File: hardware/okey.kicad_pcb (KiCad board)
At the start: 2 copper layers, 263.4 x 349.9 mm, 158 parts, among them IC1 4094N, IC2 4094N, P1 ROW_JMP, P10 CONN_02X06, P11 CONN_02X06, P12 CONN_02X06, P13 CONN_02X06, P14 CONN_02X06, P15 CONN_02X06, P16 CONN_02X08, P17 CONN_01X01, P18 CONN_02X08, P19 CONN_01X01, P2 CONN_02X13, P20 CONN_01X01, P21 CONN_01X01, P22 CONN_02X08, P23 CONN_02X08, P24 CONN_02X06, P25 CONN_02X06, P26 CONN_02X06, P27 CONN_02X06, P28 CONN_02X06, P29 CONN_02X06, P3 CONN_02X03, P30 CONN_02X08, P31 CONN_02X03, P32 CONN_02X03, P33 CONN_02X06, P34 CONN_02X06, P35 CONN_02X06, P36 CONN_02X06, P37 CONN_02X06, P38 CONN_02X06, P39 CONN_01X01, P4 CONN_02X08, P40 CONN_02X03, P41 CONN_02X06, P42 CONN_02X06, P43 CONN_02X06, P44 CONN_02X06, P45 CONN_02X06, P46 CONN_02X06, P47 CONN_01X01, P48 CONN_02X03, P5 CONN_02X03, P6 CONN_02X10, P7 CONN_02X03, P8 CONN_01X01, P9 CONN_02X08, Q1 Q_NPN_BCE, Q2 Q_NPN_BCE, Q3 Q_NPN_BCE, SW1 MX_D, SW10 MX_D, SW11 MX_D, SW12 MX_D, SW13 MX_D, SW14 MX_D, SW15 MX_D, SW16 MX_D, SW17 MX_D, SW18 MX_D, SW19 SW_PUSH, SW2 MX_D, SW20 SW_PUSH, SW21 SW_PUSH, SW22 SW_PUSH, SW23 SW_PUSH, SW24 SW_PUSH, SW25 SW_PUSH, SW26 SW_PUSH, SW27 SW_PUSH, SW28 SW_PUSH, SW29 SW_PUSH, SW3 MX_D, SW30 SW_PUSH, SW31 SW_PUSH, SW32 SW_PUSH, SW33 SW_PUSH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

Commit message: squash! ... hardware: rework SPI board as SMD board with smaller dimensions ...
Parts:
- added J1: RJ45, Connect:RJ45_8, F.Cu at (63.5, 15.2)
- added J2: RJ45, Connect:RJ45_8, F.Cu at (80.0, 15.2)
- D1, D2, D3, D4, D5, D6, D7, D8: footprint Discret:CP6 -> Discret:D3
- D10, D11, D12, D13, D14, D15, D16, D17, D18, D19, D20, D21, D22, D23, D24, D9: footprint Discret:R4 -> Discret:D4
- moved C1 30.5 mm to (62.9, 62.9)
- moved PNL_ID1 22.2 mm to (106.7, 48.3), turned to 90 degrees
- moved P48 19.4 mm to (109.2, 26.7), turned to 90 degrees
- moved C3 18.1 mm to (50.2, 64.8)
- moved C6 18.1 mm to (77.5, 62.2)
- moved C7 18.1 mm to (77.5, 62.2)
- moved D8 16.6 mm to (124.5, 39.4), turned to 270 degrees
- moved MUX_COL1 14.6 mm to (99.7, 41.3)
- moved P3 14.0 mm to (55.9, 36.8)
- moved U1 14.0 mm to (64.1, 41.3)
- moved P5 14.0 mm to (69.8, 36.8)
- moved C2 13.9 mm to (102.9, 25.4), turned to 270 degrees
- moved D7 13.1 mm to (121.9, 39.4), turned to 270 degrees
- moved P4 10.2 mm to (106.7, 33.0), turned to 90 degrees
- moved D6 9.67 mm to (119.4, 39.4), turned to 270 degrees
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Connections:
- net Net-(P3-Pad1) renamed /Panel Generic SPI01/reset
- net Net-(P3-Pad4) renamed /Panel Generic SPI01/miso
- net Net-(P3-Pad6) renamed /Panel Generic SPI01/clock
- net Net-(P5-Pad4) renamed /Panel Generic SPI01/PNL_BUS_OUT
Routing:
- net Net-(D23-Pad2): track 26.5 -> 119.8 mm
- net Net-(D23-Pad1): track 96.7 -> 7.40 mm
- net Net-(D17-Pad2): track 36.8 -> 115.6 mm
- net Net-(D19-Pad2): track 57.3 -> 117.1 mm
- net Net-(D21-Pad1): track 64.1 -> 7.40 mm
- net Net-(D21-Pad2): track 61.3 -> 118.0 mm
- net Net-(D8-Pad1): track 78.8 -> 22.1 mm
- net Net-(D17-Pad1): track 59.8 -> 7.40 mm
- net Net-(MUX_ROW1-Pad15): track 4.86 -> 53.1 mm, vias 0 -> 2
- net Net-(D19-Pad1): track 52.2 -> 7.40 mm
- net VDD: track 111.5 -> 73.8 mm, vias 1 -> 0
- net Net-(D13-Pad2): track 84.3 -> 113.1 mm
- net Net-(IC1-Pad1): track 124.6 -> 97.1 mm, vias 2 -> 4
- net Net-(D18-Pad1): track 32.1 -> 5.61 mm
- net Net-(MUX_COL1-Pad10): track 32.2 -> 7.81 mm
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
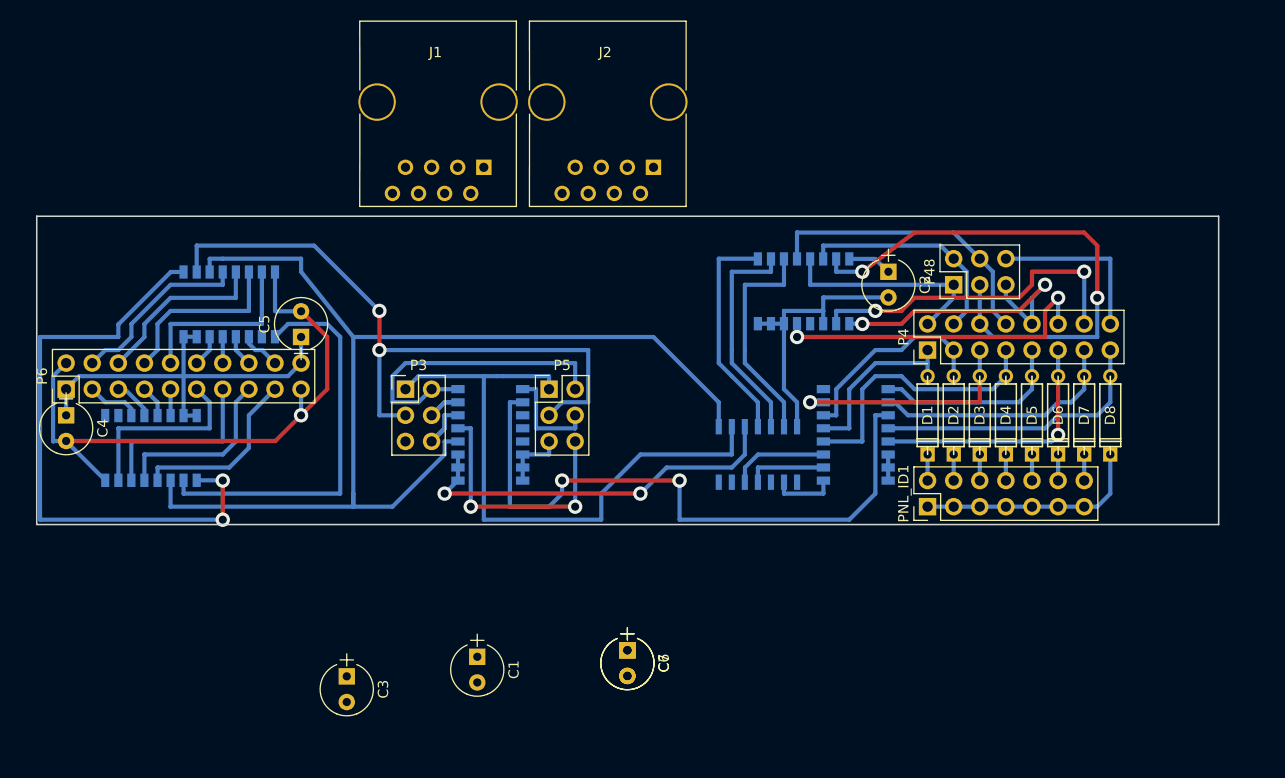
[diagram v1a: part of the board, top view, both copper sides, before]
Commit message: squash! ... hardware: rework SPI board as SMD board with smaller dimensions ...
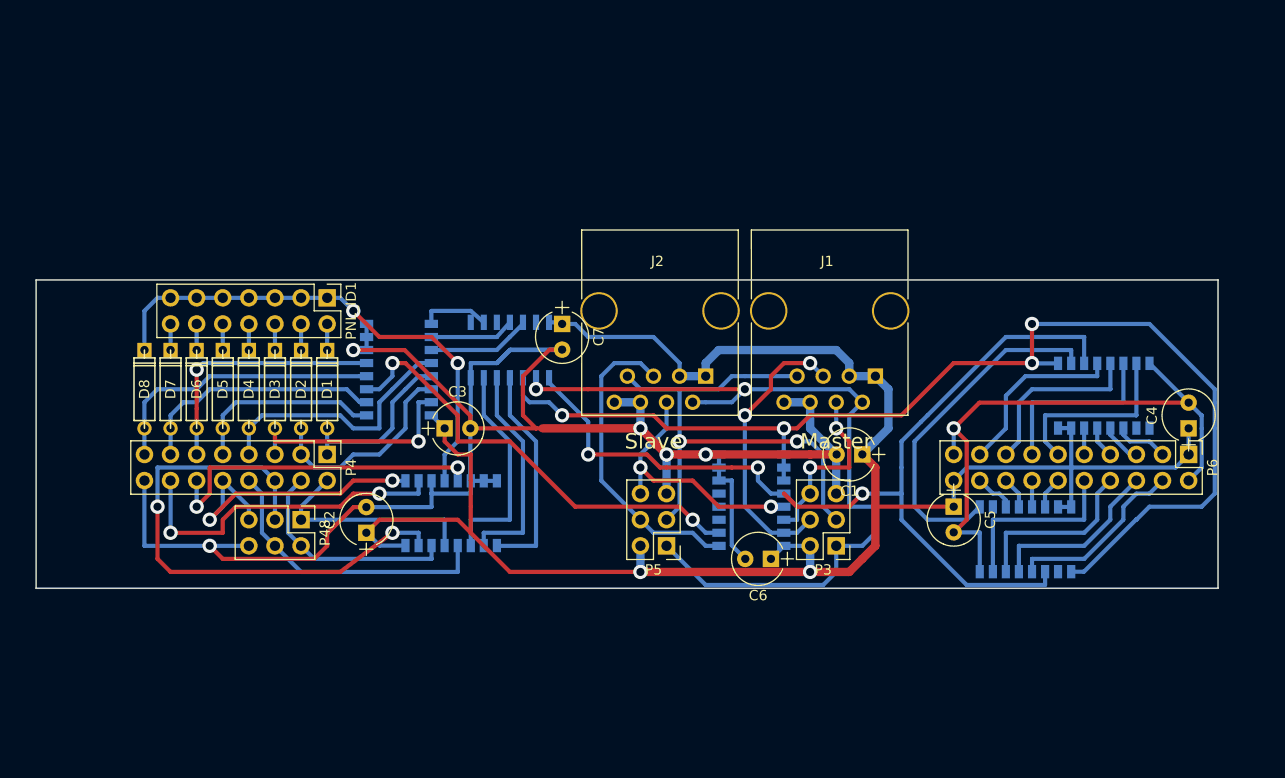
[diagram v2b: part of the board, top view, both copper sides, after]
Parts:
- moved P6 109.4 mm to (132.1, 43.2), turned to 270 degrees
- moved C4 109.2 mm to (132.1, 40.6), turned to 90 degrees
- moved D8 94.0 mm to (30.5, 36.8), turned to 90 degrees
- moved IC2 92.8 mm to (123.8, 37.5), turned to 270 degrees
- moved D7 88.9 mm to (33.0, 36.8), turned to 90 degrees
- moved D6 83.9 mm to (35.6, 36.8), turned to 90 degrees
- moved IC1 80.8 mm to (116.2, 51.4), turned to 90 degrees
- moved D5 78.8 mm to (38.1, 36.8), turned to 90 degrees
- moved D4 73.7 mm to (40.6, 36.8), turned to 90 degrees
- moved D3 68.6 mm to (43.2, 36.8), turned to 90 degrees
- moved P48 67.5 mm to (45.7, 49.5), turned to 270 degrees
- moved C5 65.6 mm to (109.2, 48.3), turned to 270 degrees
- moved D2 63.6 mm to (45.7, 36.8), turned to 90 degrees
- moved PNL_ID1 61.9 mm to (48.3, 27.9), turned to 270 degrees
- moved P4 59.3 mm to (48.3, 43.2), turned to 270 degrees
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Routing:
- net GND: track 112.4 -> 238.3 mm, vias 1 -> 6
- net VDD: track 73.8 -> 184.5 mm, vias 0 -> 2
- net Net-(D8-Pad1): track 22.1 -> 49.4 mm, vias 0 -> 2
- net /Panel Generic SPI01/miso: track 6.18 -> 27.8 mm, vias 0 -> 2
- net /Panel Generic SPI01/reset: track 60.7 -> 80.2 mm, vias 0 -> 2
- net /Panel Generic SPI01/PNL_BUS_OUT: track 11.5 -> 30.4 mm
- net Net-(MUX_COL1-Pad3): track 63.1 -> 44.4 mm
- net Net-(IC1-Pad1): track 97.1 -> 114.4 mm
- net Net-(IC1-Pad3): track 111.8 -> 94.7 mm, vias 0 -> 3
- net Net-(IC1-Pad2): track 65.4 -> 52.2 mm
- net /Panel Generic SPI01/clock: track 7.44 -> 17.6 mm, vias 0 -> 2
- net Net-(IC1-Pad9): track 39.2 -> 34.0 mm
- net Net-(D4-Pad2): track 27.0 -> 25.5 mm
- net Net-(D1-Pad2): track 17.5 -> 16.8 mm
- net Net-(MUX_COL1-Pad9): track 6.20 -> 6.77 mm
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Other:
- outline, holes or cut-outs redrawn
- board text added: "Master"
- board text added: "Slave"

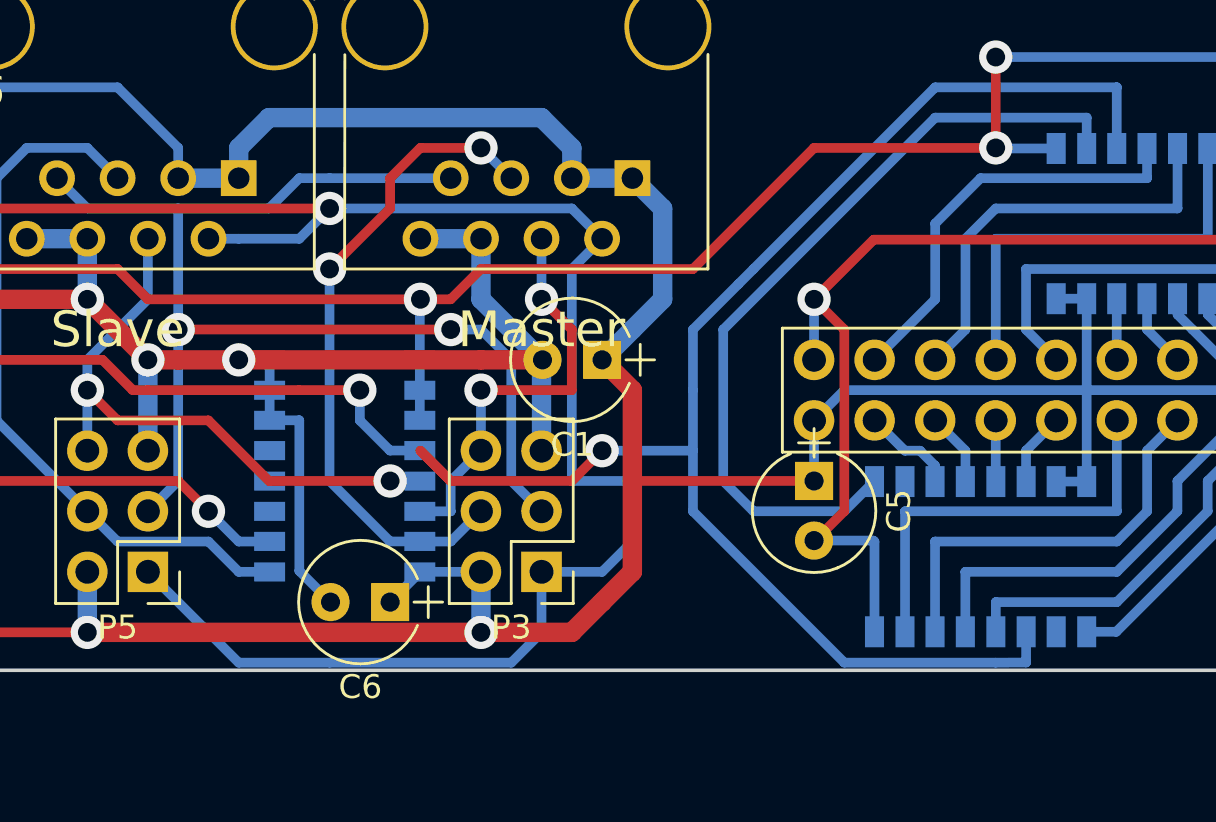
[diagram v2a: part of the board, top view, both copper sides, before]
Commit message: squash! ... hardware: rework SPI board as SMD board with smaller dimensions: all lines connected ...
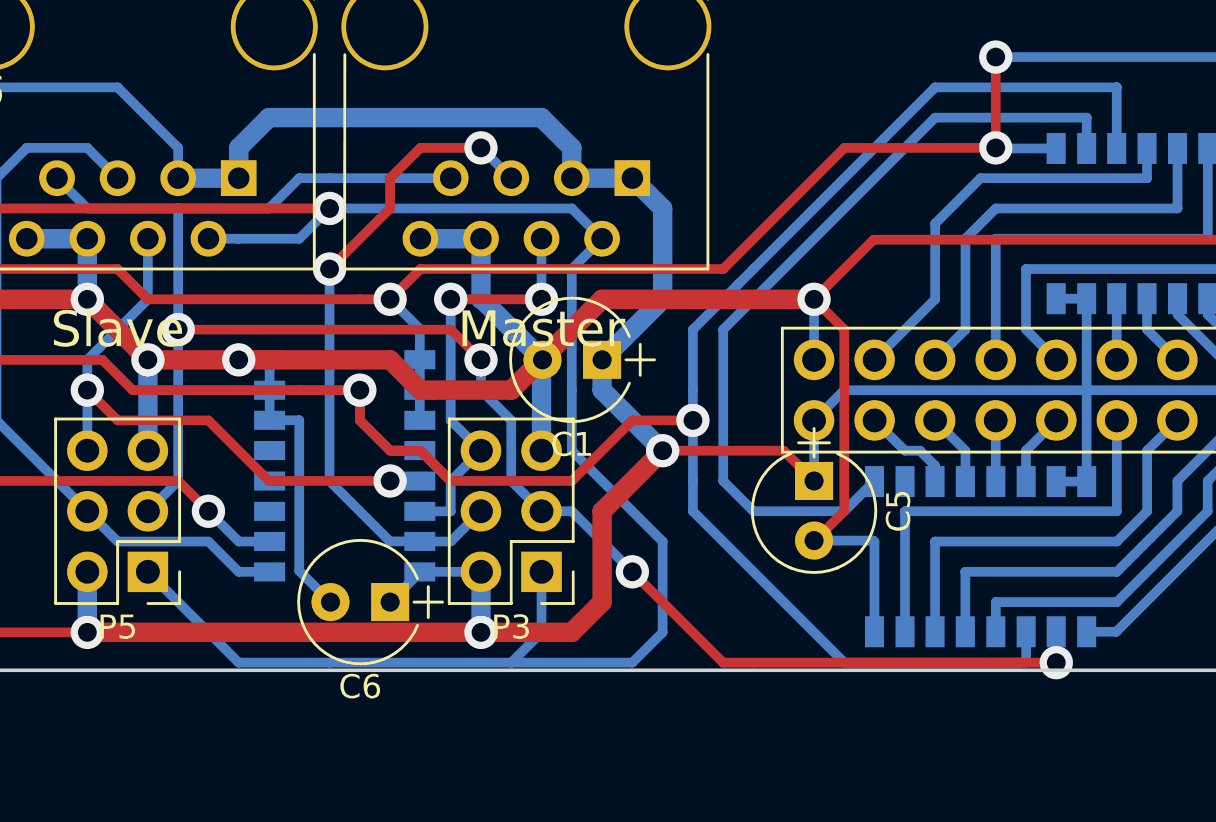
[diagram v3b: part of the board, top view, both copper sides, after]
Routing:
- net Net-(IC1-Pad2): track 52.2 -> 76.9 mm, vias 2 -> 4
- net GND: track 238.3 -> 252.0 mm
- net /Panel Generic SPI01/reset: track 80.2 -> 85.6 mm
- net Net-(IC1-Pad3): track 94.7 -> 99.6 mm
- net Net-(IC1-Pad1): track 114.4 -> 114.9 mm
- net VDD: track 184.5 -> 184.8 mm, vias 2 -> 3

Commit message: ...
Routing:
- net /Panel Generic SPI01/reset: track 85.6 -> 99.4 mm, vias 2 -> 0
- net Net-(D8-Pad2): track 27.7 -> 26.3 mm
- net Net-(D6-Pad2): track 25.1 -> 23.9 mm
- net Net-(D7-Pad2): track 24.5 -> 23.7 mm
- net Net-(IC1-Pad3): track 99.6 -> 100.2 mm

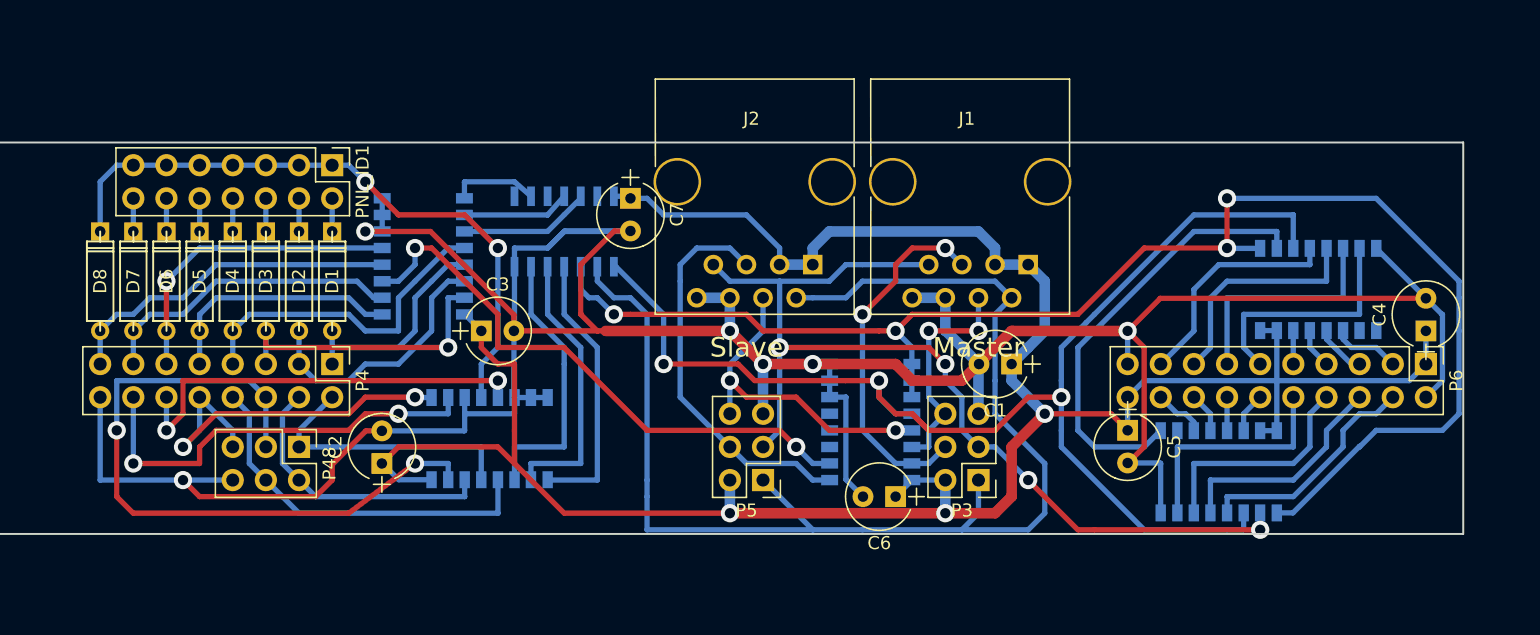
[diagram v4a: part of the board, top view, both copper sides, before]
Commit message: squash! ... hardware: rework SPI board as SMD board with smaller dimensions: pin header or rj45 connector options ...
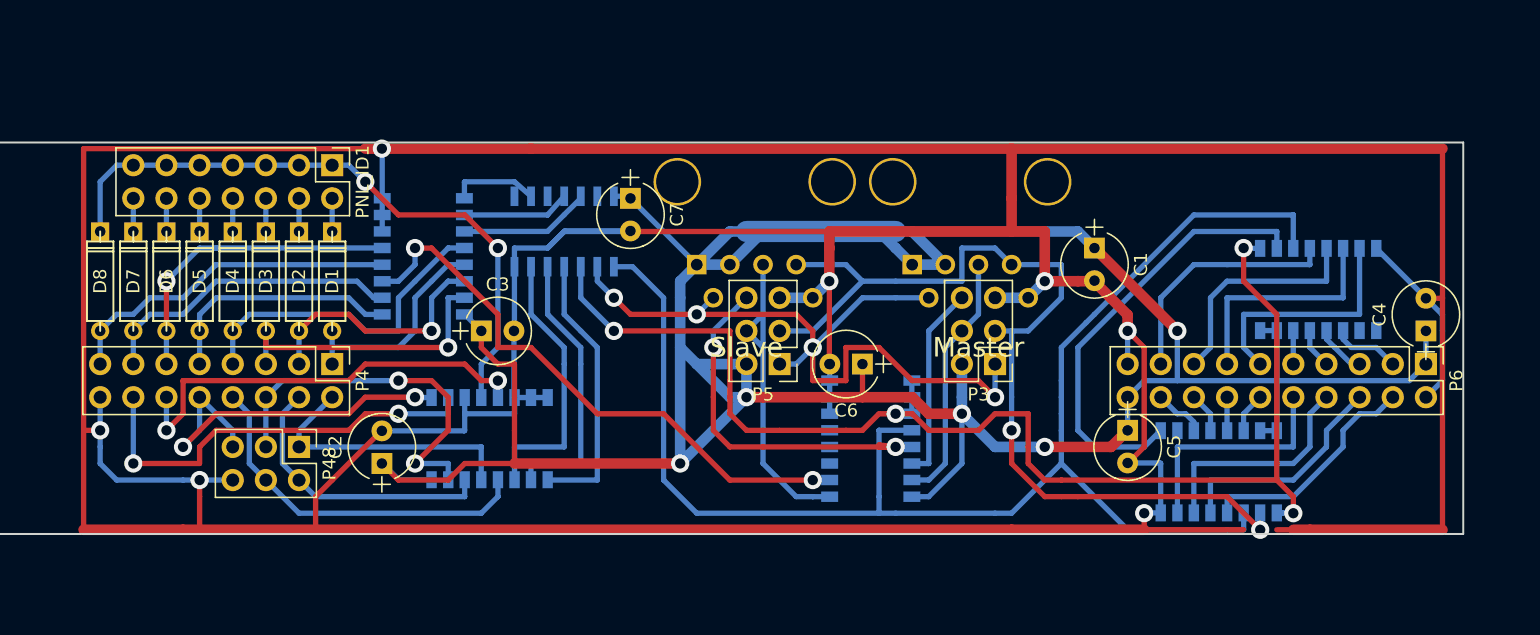
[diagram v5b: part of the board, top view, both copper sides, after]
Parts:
- J1, J2: moved to B.Cu
- moved C1 10.9 mm to (106.7, 34.3), turned to 270 degrees
- moved C6 10.5 mm to (88.9, 43.2)
- moved P3 8.98 mm to (99.1, 43.2)
- moved P5 8.98 mm to (82.5, 43.2)
- moved J1 8.89 mm to (92.7, 35.6), turned to 0 degrees
- moved J2 8.89 mm to (76.2, 35.6), turned to 0 degrees
- moved U1 1.27 mm to (89.5, 48.9)
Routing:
- net GND: track 252.0 -> 456.7 mm, vias 6 -> 8
- net VDD: track 184.8 -> 245.5 mm, vias 3 -> 5
- net /Panel Generic SPI01/reset: track 99.4 -> 59.0 mm, vias 0 -> 4
- net Net-(MUX_ROW1-Pad15): track 53.1 -> 28.8 mm
- net Net-(IC1-Pad1): track 114.9 -> 99.0 mm
- net Net-(IC1-Pad3): track 100.2 -> 112.2 mm, vias 3 -> 0
- net /Panel Generic SPI01/miso: track 27.8 -> 19.4 mm, vias 2 -> 0
- net /Panel Generic SPI01/PNL_BUS_OUT: track 30.4 -> 25.0 mm
- net Net-(J2-Pad4): track 25.5 -> 29.7 mm
- net Net-(IC1-Pad2): track 76.9 -> 73.1 mm, vias 4 -> 2
- net /Panel Generic SPI01/clock: track 17.6 -> 15.0 mm, vias 2 -> 0
- net Net-(IC2-Pad4): track 17.7 -> 18.8 mm
- net Net-(MUX_ROW1-Pad5): track 32.3 -> 33.4 mm
- net Net-(D2-Pad2): track 20.4 -> 19.3 mm, vias 0 -> 1
- net Net-(MUX_ROW1-Pad12): track 28.8 -> 28.1 mm
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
